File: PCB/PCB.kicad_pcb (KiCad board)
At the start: 2 copper layers, 87 x 37 mm, 2 parts, among them J1 Conn_01x08, U1 RASPBERRY_PI_ZERO_2_W

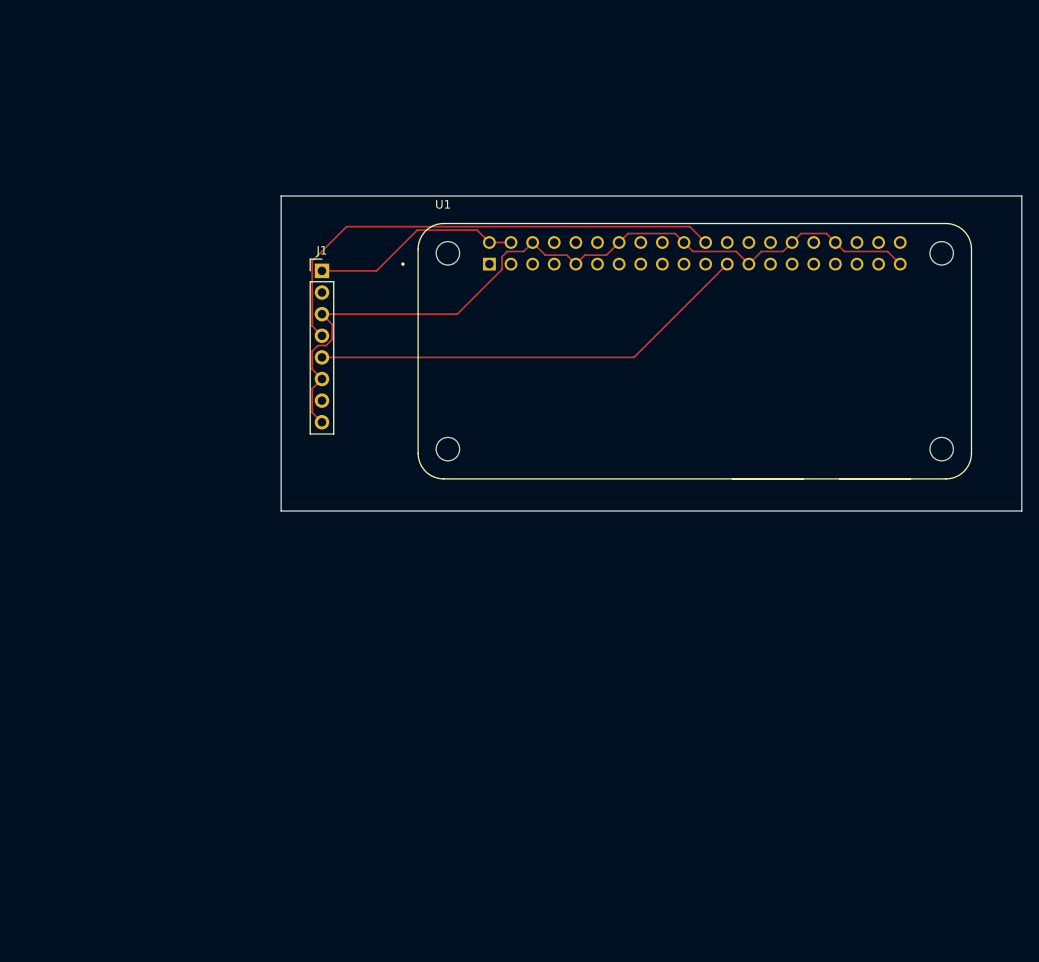
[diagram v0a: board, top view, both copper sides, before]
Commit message: finnished PCB and did a notes.md
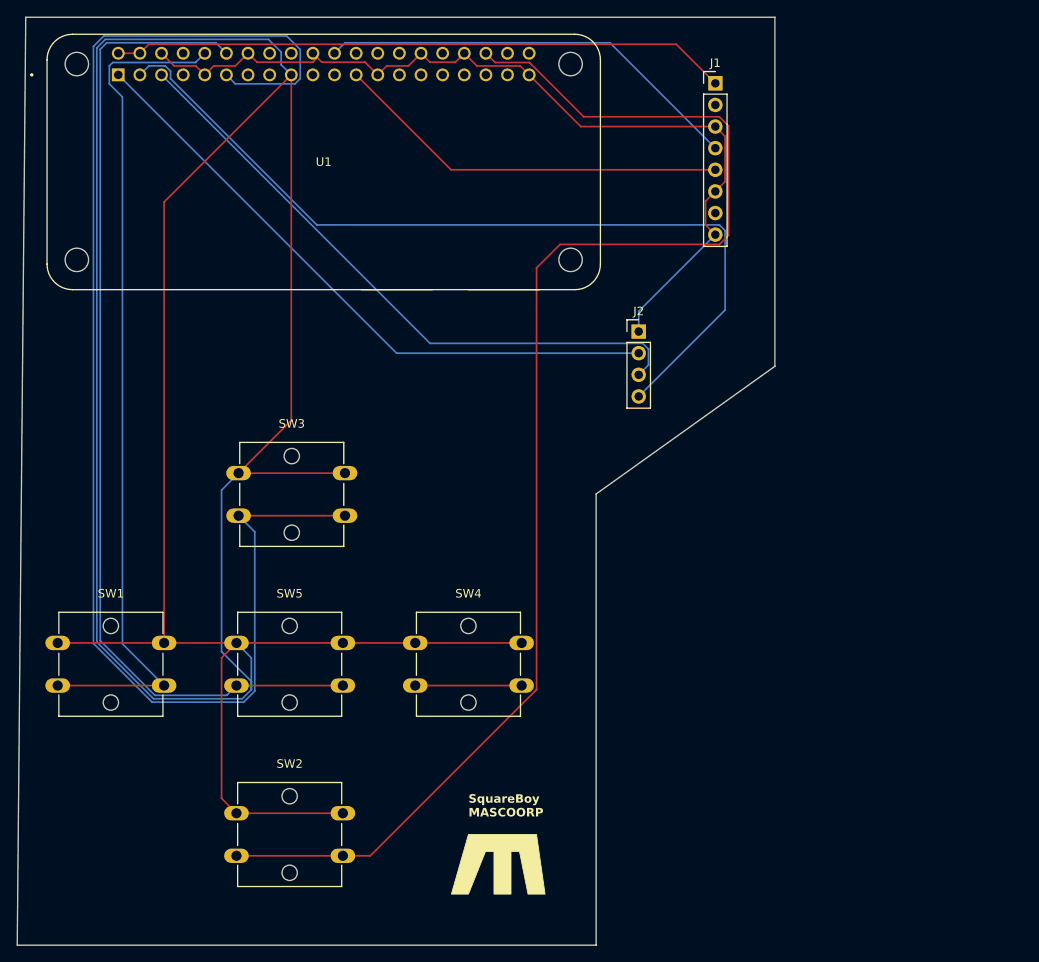
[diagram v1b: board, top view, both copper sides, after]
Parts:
- added J2: I2C display <-, Connector_PinHeader_2.54mm:PinHeader_1x04_P2.54mm_Vertical, F.Cu at (140.0, 60.9)
- added SW1: SW_Push, Button_Switch_THT:SW_SPST_Omron_B3F-40xx, F.Cu at (71.8, 97.5)
- added SW2: SW_Push, Button_Switch_THT:SW_SPST_Omron_B3F-40xx, F.Cu at (92.8, 117.5)
- added SW3: SW_Push, Button_Switch_THT:SW_SPST_Omron_B3F-40xx, F.Cu at (93.0, 77.5)
- added SW4: SW_Push, Button_Switch_THT:SW_SPST_Omron_B3F-40xx, F.Cu at (113.8, 97.5)
- added SW5: SW_Push, Button_Switch_THT:SW_SPST_Omron_B3F-40xx, F.Cu at (92.8, 97.5)
- J1: value Conn_01x08 -> USB_C BREAKOUT ->
- moved J1 51.2 mm to (149.0, 31.8)
- moved U1 48.9 mm to (103.0, 41.0)
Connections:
- U1 pad 1: unconnected-(U1-3V3_1-Pad1) -> Net-(J2-Pin_2)
- U1 pad 10: unconnected-(U1-GPIO15/RXD0-Pad10) -> Net-(U1-GPIO15/RXD0)
- U1 pad 11: unconnected-(U1-GPIO17/GPIO_GEN0-Pad11) -> Net-(U1-GPIO17/GPIO_GEN0)
- U1 pad 12: unconnected-(U1-GPIO18/GPIO_GEN1-Pad12) -> Net-(U1-GPIO18/GPIO_GEN1)
- U1 pad 17: unconnected-(U1-3V3_17-Pad17) -> Net-(U1-3V3_17)
- U1 pad 3: unconnected-(U1-GPIO2/SDA1-Pad3) -> Net-(J2-Pin_4)
- U1 pad 36: unconnected-(U1-GPIO16-Pad36) -> Net-(U1-GPIO16)
- U1 pad 5: unconnected-(U1-GPIO3/SCL-Pad5) -> Net-(J2-Pin_3)
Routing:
- net Net-(U1-3V3_17): track 0.00 -> 374.5 mm
- net Net-(U1-GPIO17/GPIO_GEN0): track 0.00 -> 164.6 mm
- net Net-(U1-GPIO16): track 0.00 -> 161.9 mm
- net Net-(U1-GPIO18/GPIO_GEN1): track 0.00 -> 116.7 mm
- net Net-(J2-Pin_4): track 0.00 -> 101.4 mm
- net Net-(U1-GPIO15/RXD0): track 0.00 -> 99.8 mm
- net Net-(J2-Pin_2): track 0.00 -> 74.7 mm
- net Net-(J2-Pin_3): track 0.00 -> 74.0 mm
- net Net-(J1-Pin_1): track 24.8 -> 72.5 mm
- net unconnected-(SW4-Pad2): track 0.00 -> 12.5 mm
- net Net-(J1-Pin_3): track 95.5 -> 104.6 mm
- net Net-(J1-Pin_4): track 57.9 -> 50.4 mm
- net Net-(J1-Pin_5): track 52.1 -> 46.8 mm
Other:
- board size 87 x 37 mm -> 89 x 109 mm
- board text added: "SquareBoy MASCOORP"

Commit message: added the brand silkscreeen
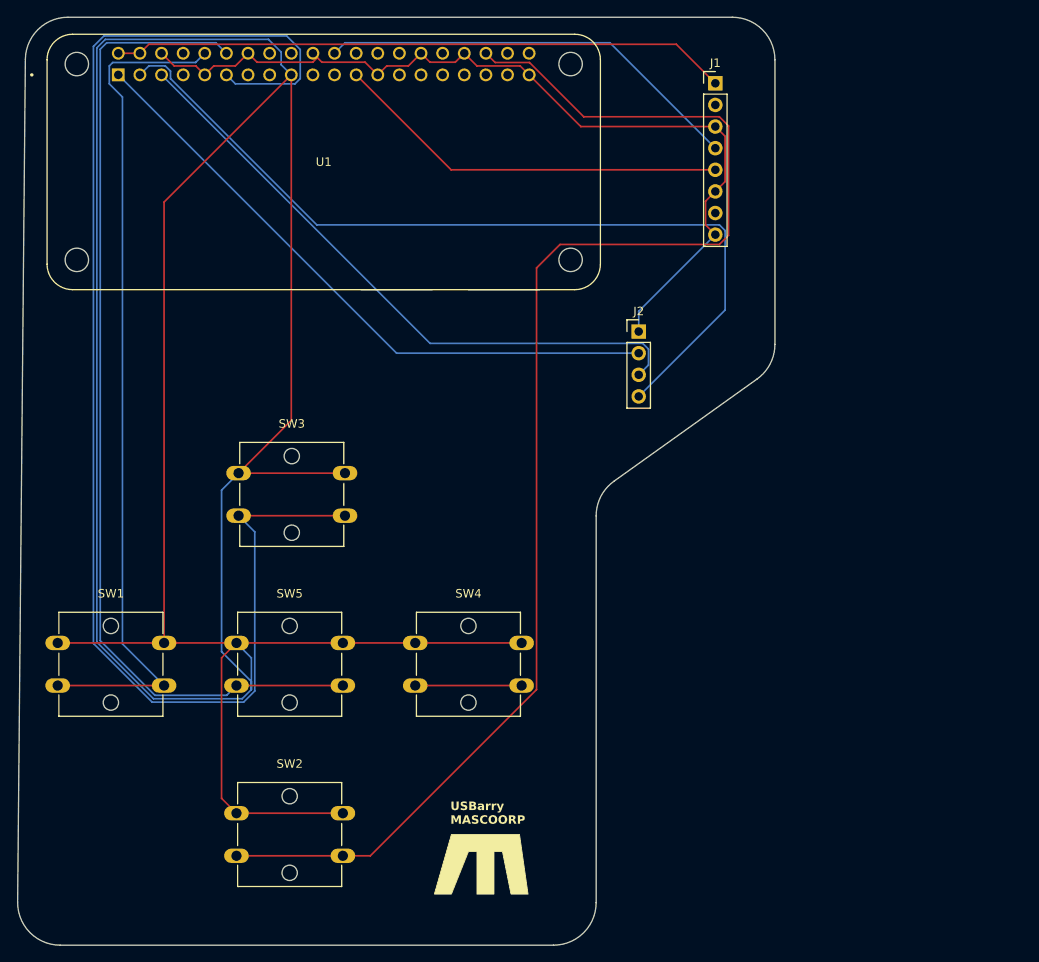
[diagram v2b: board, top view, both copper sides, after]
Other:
- outline, holes or cut-outs redrawn
- board text added: "USBarry MASCOORP"
- board text removed: "SquareBoy MASCOORP"

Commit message: rewired
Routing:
- net Net-(U1-3V3_17): track 374.5 -> 274.3 mm
- net Net-(U1-GPIO17/GPIO_GEN0): track 164.6 -> 126.3 mm
- net Net-(U1-GPIO16): track 161.9 -> 129.8 mm
- net Net-(J2-Pin_4): track 101.4 -> 83.5 mm
- net Net-(U1-GPIO18/GPIO_GEN1): track 116.7 -> 125.2 mm
- net Net-(U1-GPIO15/RXD0): track 99.8 -> 95.4 mm
- net Net-(J1-Pin_4): track 50.4 -> 53.6 mm
- net Net-(J1-Pin_3): track 104.6 -> 105.9 mm
- net Net-(J1-Pin_1): track 72.5 -> 73.4 mm
